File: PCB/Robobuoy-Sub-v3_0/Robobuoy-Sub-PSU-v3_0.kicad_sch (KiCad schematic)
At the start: 83 parts, among them J301 CHRG/DATA, J302 ESC_SB, J303 ESC_BB, J304 ESC_PWR_SB, J305 ESC_PWR_BB, J306 ACCU2, J307 ACCU2, Q301 AO3400A, Q302 AO3401A, Q303 AO3401A, Q304 AO3400A, Q305 AO3400A, Q306 HYG025N04NA1C2, Q307 HYG025N04NA1C2, SW301 On/Off, U301 SN74LV1T34DBV, U302 SN74LV1T34DBV, U303 LMR16020PDDA

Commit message: PCB changes
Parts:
- removed C309: 10u/25V, A_Device:C_0805, symbol Device:C_Small
- removed C315: 100u/10V, Capacitor_SMD:C_1210_3225Metric, symbol Device:C_Small
- removed C317: 100n, A_Device:C_0603, symbol Device:C_Small
- removed J307: ACCU2, A_Connector:AMASS_XT60IPW-M_1x03_P7.20mm_Horizontal, symbol Connector:Conn_01x02_Socket
- removed Q306, Q307: HYG025N04NA1C2, Package_DFN_QFN:PQFN-8-EP_6x5mm_P1.27mm_Generic, symbol Transistor_FET:BSC082N10LSG
- added Q306, Q308: AON6407-MS, Package_DFN_QFN:AO_DFN-8-1EP_5.55x5.2mm_P1.27mm_EP4.12x4.6mm, symbol Transistor_FET:AON6411
- C308: value 10u/25V -> 100n; footprint A_Device:C_0805 -> A_Device:C_0603; LCSC C15850 -> C14663
- J301: footprint A_Connector:AMASS_XT60IPW-M_1x03_P5.50mm_Vertical -> RoundWire_1x03_P5.50mm_Vertical
- J304, J305: footprint A_Connector:AMASS_XT60PW-F_1x02_P7.20mm_Horizontal -> Connector_AMASS:AMASS_XT30U-M_1x02_P5.0mm_Vertical
- J306: footprint A_Connector:AMASS_XT60IPW-M_1x03_P7.20mm_Horizontal -> Connector_AMASS:AMASS_XT30U-M_1x02_P5.0mm_Vertical
- renumbered C310 to C309, C311 to C310, C312 to C311, C313 to C312, C314 to C313, C316 to C315, C318 to C317
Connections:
- net Vbatt: now also Q306.1 (S), Q306.2 (S), Q306.3 (S), Q308.1 (S), Q308.2 (S), Q308.3 (S)
- net buck_sw: now reaches C311.1, D307.1 (K), L301.1, U303.8 (SW)
- net at R326.2, R328.2: now also Q306.4 (G)
- net at R325.2, R327.2: now also Q308.4 (G)
- net at J304.2 (Pin_2): now also Q308.5 (D)
- net at J305.2 (Pin_2): now also Q306.5 (D)
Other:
- moved on the sheet: TP303

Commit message: PCB 3.0 almoste finished Imon calculation added
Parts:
- added C314: 100n, A_Device:C_0603, symbol Device:C_Small
- added R330, R337, R338, R339: 1, Resistor_SMD:R_2512_6332Metric_Pad1.40x3.35mm_HandSolder, symbol Device:R_Small
- added R331, R332: 1.5K, A_Device:R_0603, symbol Device:R_Small
- added R333, R334: 4.6K, A_Device:R_0603, symbol Device:R_Small
- added R335, R336: 10K, A_Device:R_0603, symbol Device:R_Small
- added U304: TL082, Package_SO:SO-8_3.9x4.9mm_P1.27mm, symbol Amplifier_Operational:TL082
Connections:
- net GND: now also C314.2, R330.1, R331.1, R336.1, R337.1, R338.1, R339.1, U304.4 (V-); no longer J306.1 (Pin_1)
- new net: R332.2, R333.1, U304.6 (-)
- new net: R334.2, U304.1, U304.2 (-)
- new net: R335.1, R336.2, U304.3 (+)
- new net: R331.2, R334.1, U304.5 (+)
- new net +3.3V: C314.1, R335.2, U304.8 (V+)
- new net GND1: J306.1 (Pin_1), R330.2, R332.1, R337.2, R338.2, R339.2
- new net Imon: R333.2, U304.7
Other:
- moved on the sheet: J306

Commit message: pcb ready for production
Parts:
- removed J306: ACCU2, Connector_AMASS:AMASS_XT30U-M_1x02_P5.0mm_Vertical, symbol Connector:Conn_01x02_Socket
- removed TP309: GND, TestPoint:TestPoint_Loop_D2.54mm_Drill1.5mm_Beaded, symbol Connector:TestPoint
- added J306: LiPo S6, symbol NicE:LiPo
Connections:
- net GND: now also R332.1; no longer R331.1
- net Vbatt: now also J306.2 (+)
- net GND1: no longer names the net of R330.2, R337.2, R338.2, R339.2
- net GND1: now also R331.1, J306.1 (-); no longer R332.1
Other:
- moved on the sheet: R330, R337, R338, R339

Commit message: Last cosmetic cleanupt
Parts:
- J302, J303, SW301: now not fitted
- TP302: value Vcell -> VSAMP
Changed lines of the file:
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@@
 			)
 		)
-		(property "Value" "Vcell"
+		(property "Value" "VSAMP"
 			(at 111.76 134.62 0)
 			(effects
@@
 		(in_bom yes)
 		(on_board yes)
-		(dnp no)
+		(dnp yes)
 		(fields_autoplaced yes)
 		(property "Reference" "J302"
@@
 		(in_bom yes)
 		(on_board yes)
-		(dnp no)
+		(dnp yes)
 		(property "Reference" "SW301"
 			(at 87.884 253.238 0)
@@
 		(in_bom yes)
 		(on_board yes)
-		(dnp no)
+		(dnp yes)
 		(fields_autoplaced yes)
 		(property "Reference" "J303"

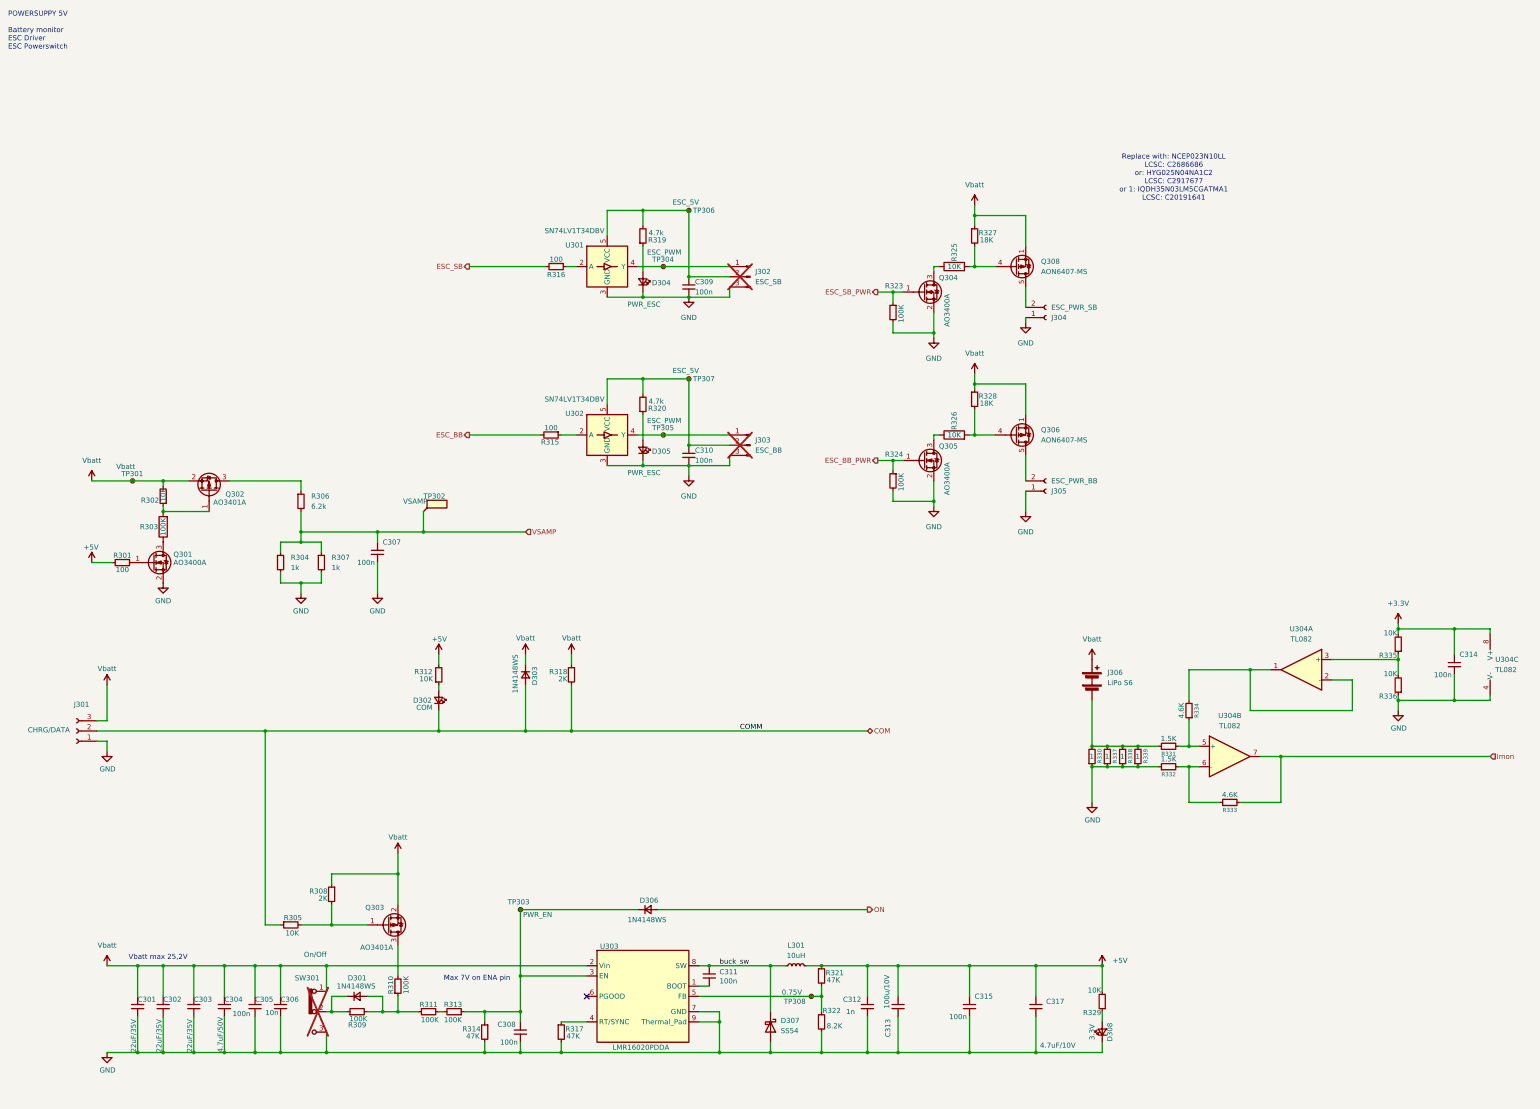
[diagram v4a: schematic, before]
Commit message: Simulation added bms Little improvements BMS Resistor divider added on the gate of the mosfet (Limmeded to +/-20V could be 30V during charging)
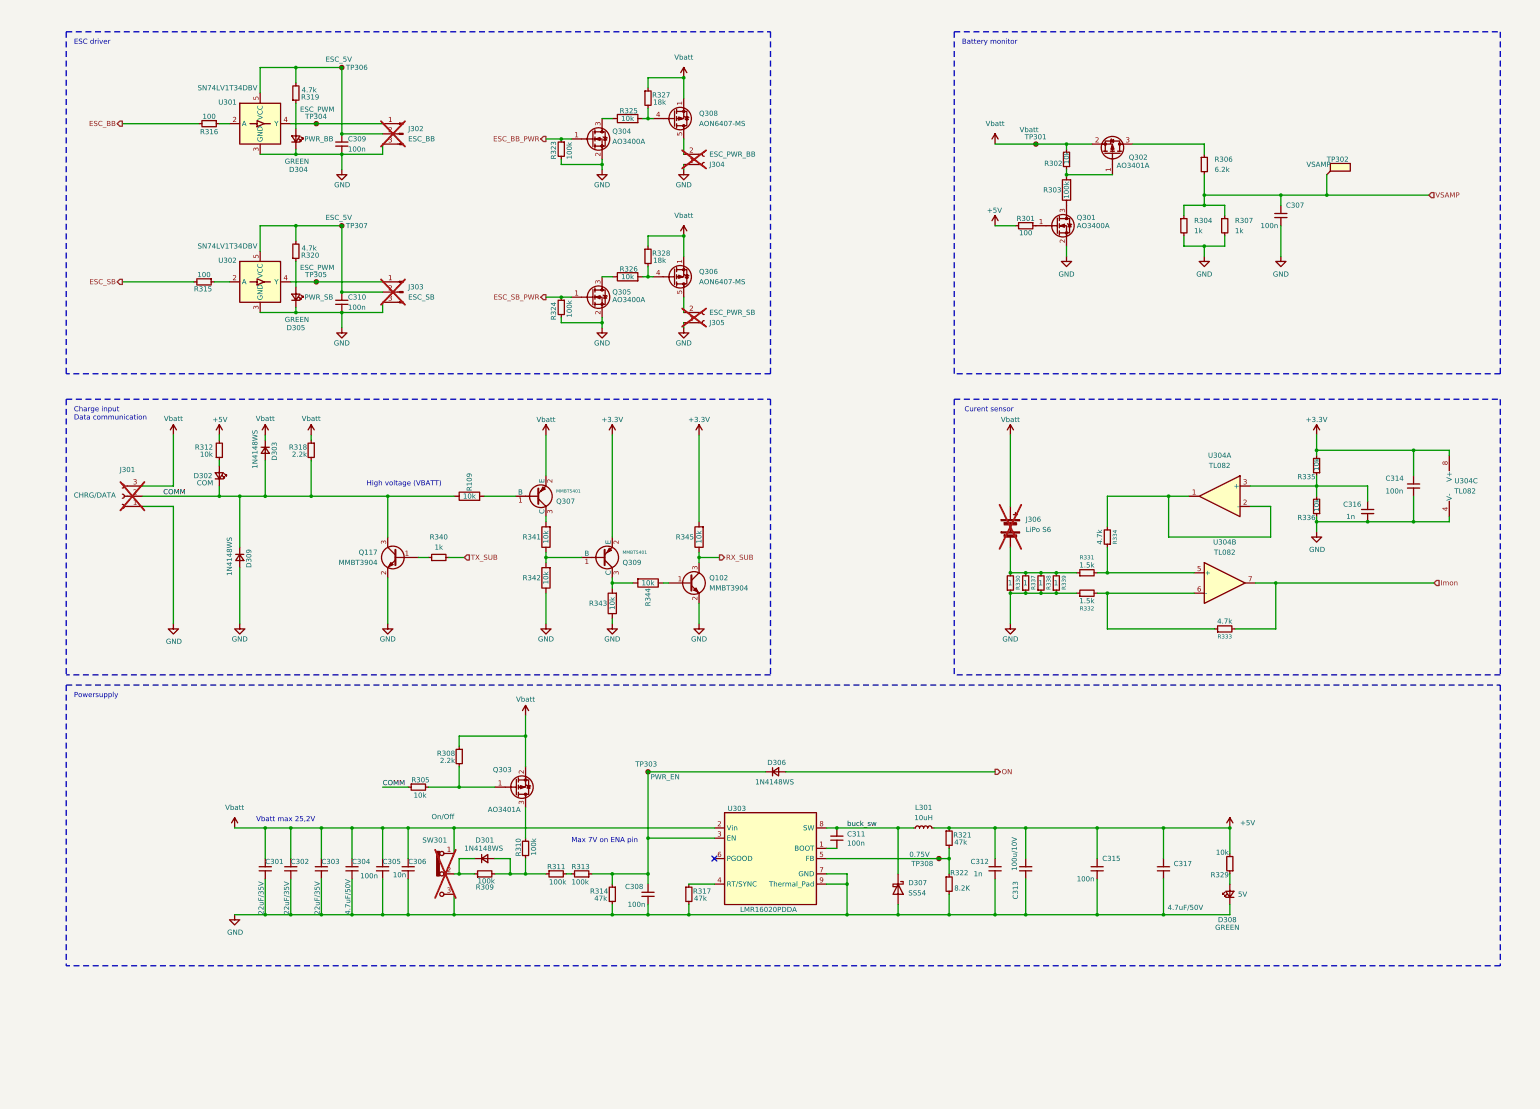
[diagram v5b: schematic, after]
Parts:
- added C316: 1n, A_Device:C_0603, symbol Device:C_Small
- added D309: 1N4148WS, A_Device:D_SOD-323_1.8x1.4x1.15, symbol Device:D_Small
- added Q102, Q117: MMBT3904, Package_TO_SOT_SMD:SOT-23, symbol Transistor_BJT:BC847
- added Q307, Q309: MMBT5401, PCM_JLCPCB:Q_SOT-23, symbol PCM_JLCPCB-Transistors:PNP,MMBT5401
- added R109, R341, R342, R343, R344, R345: 10k, A_Device:R_0603, symbol Device:R
- added R340: 1k, A_Device:R_0603, symbol Device:R_Small
- C317: value 4.7uF/10V -> 4.7uF/50V
- D304: value PWR_ESC -> GREEN; Text (none) -> PWR_BB
- D305: value PWR_ESC -> GREEN; Text (none) -> PWR_SB
- D308: value 3.3V -> GREEN; footprint A_Passive:LED_0805 -> LED_SMD:LED_0603_1608Metric; LCSC C2297 -> C2286; Text (none) -> 5V
- J301, J306: now not fitted; now left out of the parts list
- J302: value ESC_SB -> ESC_BB; now left out of the parts list
- J303: value ESC_BB -> ESC_SB; now left out of the parts list
- J304: value ESC_PWR_SB -> ESC_PWR_BB; now not fitted; now left out of the parts list
- J305: value ESC_PWR_BB -> ESC_PWR_SB; now not fitted; now left out of the parts list
- R302, R305, R312, R325, R326, R329, R335, R336: value 10K -> 10k
- R303, R309, R310, R311, R313, R323, R324: value 100K -> 100k
- R306: LCSC C25804 -> C4260
- R308, R318: value 2K -> 2.2k; LCSC C22975 -> C4190
- R314, R317, R321: value 47K -> 47k
- R327, R328: value 18K -> 18k
- R331, R332: value 1.5K -> 1.5k
- R333, R334: value 4.6K -> 4.7k; LCSC (none) -> C4177
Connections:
- net +3.3V: now also Q309.2 (E), R345.2
- net ESC_BB: now also R316.2; no longer R315.2
- net ESC_BB_PWR: now also Q304.1 (G), R323.1; no longer Q305.1 (G), R324.1
- net ESC_SB: now also R315.2; no longer R316.2
- net ESC_SB_PWR: now also Q305.1 (G), R324.1; no longer Q304.1 (G), R323.1
- net GND: now also C316.2, D309.2 (A), Q102.2 (E), Q117.2 (E), R342.1, R343.1
- net Vbatt: now also Q307.2 (E)
- net at R335.1, R336.2, U304.3 (+): now also C316.1
- net COM renamed COMM
- net COMM: now also D309.1 (K), Q117.3 (C), R109.1
- new net: Q309.1 (B), R341.1, R342.2
- new net: Q309.3 (C), R343.2, R344.2
- new net: Q102.1 (B), R344.1
- new net: Q307.3 (C), R341.2
- new net: Q117.1 (B), R340.1
- new net: Q307.1 (B), R109.2
- new net RX_SUB: Q102.3 (C), R345.1
- new net TX_SUB: R340.2
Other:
- note added: "Battery monitor"
- note added: "Charge input Data communication"
- note added: "Curent sensor"
- note added: "ESC driver"
- note added: "High voltage (VBATT)"
- note added: "Powersupply"
- note removed: "POWERSUPPY 5V Battery monitor ESC Driver ESC Powerswitch"
- note removed: "Replace with: NCEP023N10LL LCSC: C2686686 or: HYG025N04NA1C2 LCSC: C2917677 or 1: IQDH35N03LM5CGATMA1 LCSC: C20191641"
- moved on the sheet: C301, C302, C303, C304, C305, C306, C307, C308, C309, C310, C311, C312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

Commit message: Heel veel AI veranderingen.
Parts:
- added D310: 1N4148WS, A_Device:D_SOD-323_1.8x1.4x1.15, symbol Device:D_Small
- added R346: 100, A_Device:R_0603, symbol Device:R_Small
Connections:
- net +3.3V: now also D310.1 (K); no longer C314.1, U304.8 (V+)
- net +5V: now also C314.1, U304.8 (V+)
- net Imon: now also D310.2 (A), R346.1; no longer R333.2, U304.7
- new net: R333.2, R346.2, U304.7
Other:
- note added: "Imon 0.10V = -20A 1.65V = 0A 3.20V = 20A"

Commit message: BMS asd SUB orderd at JLCPCB
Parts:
- D304, D305, D308: LCSC C2286 -> C12624
- R303, R309, R310, R311, R313, R323, R324: LCSC C25804 -> C25803
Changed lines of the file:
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@@
 			)
 		)
-		(property "LCSC" "C25804"
+		(property "LCSC" "C25803"
 			(at 129.286 227.076 0)
 			(effects
@@
 			)
 		)
-		(property "LCSC" "C25804"
+		(property "LCSC" "C25803"
 			(at 159.004 227.076 0)
 			(effects
@@
 			)
 		)
-		(property "LCSC" "C25804"
+		(property "LCSC" "C25803"
 			(at 276.86 57.15 0)
 			(effects
@@
 			)
 		)
-		(property "LCSC" "C2286"
+		(property "LCSC" "C12624"
 			(at 85.09 83.82 0)
 			(effects
@@
 			)
 		)
-		(property "LCSC" "C25804"
+		(property "LCSC" "C25803"
 			(at 147.066 227.584 0)
 			(effects
@@
 			)
 		)
-		(property "LCSC" "C25804"
+		(property "LCSC" "C25803"
 			(at 142.494 223.774 0)
 			(effects
@@
 			)
 		)
-		(property "LCSC" "C25804"
+		(property "LCSC" "C25803"
 			(at 150.876 44.196 0)
 			(effects
@@
 			)
 		)
-		(property "LCSC" "C25804"
+		(property "LCSC" "C25803"
 			(at 150.876 83.566 0)
 			(effects
@@
 			)
 		)
-		(property "LCSC" "C2286"
+		(property "LCSC" "C12624"
 			(at 317.5 232.41 0)
 			(effects
@@
 			)
 		)
-		(property "LCSC" "C2286"
+		(property "LCSC" "C12624"
 			(at 85.09 44.45 0)
 			(effects

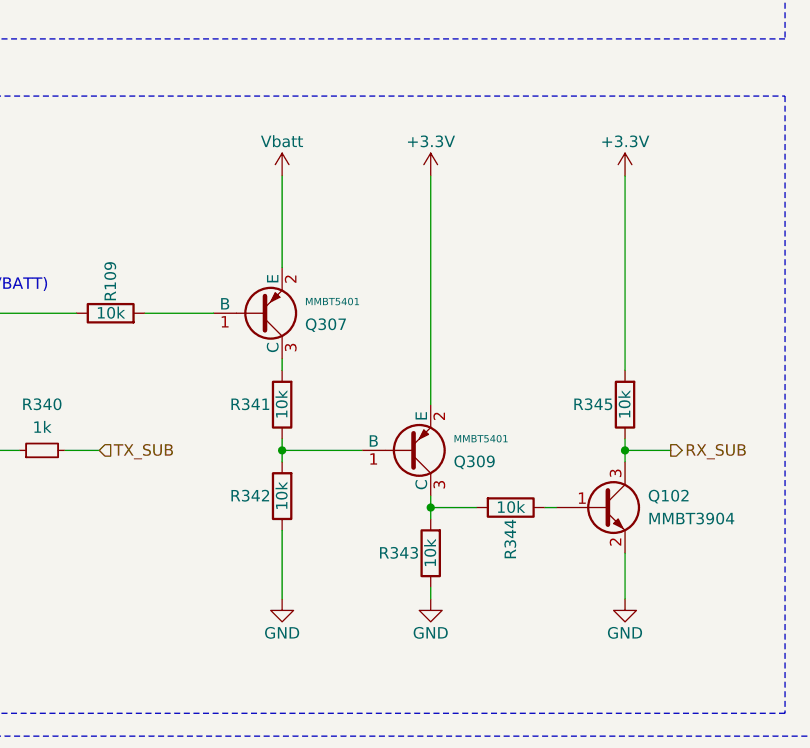
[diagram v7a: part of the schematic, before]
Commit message: docs: update PCB schematics and add ICM20948 datasheet
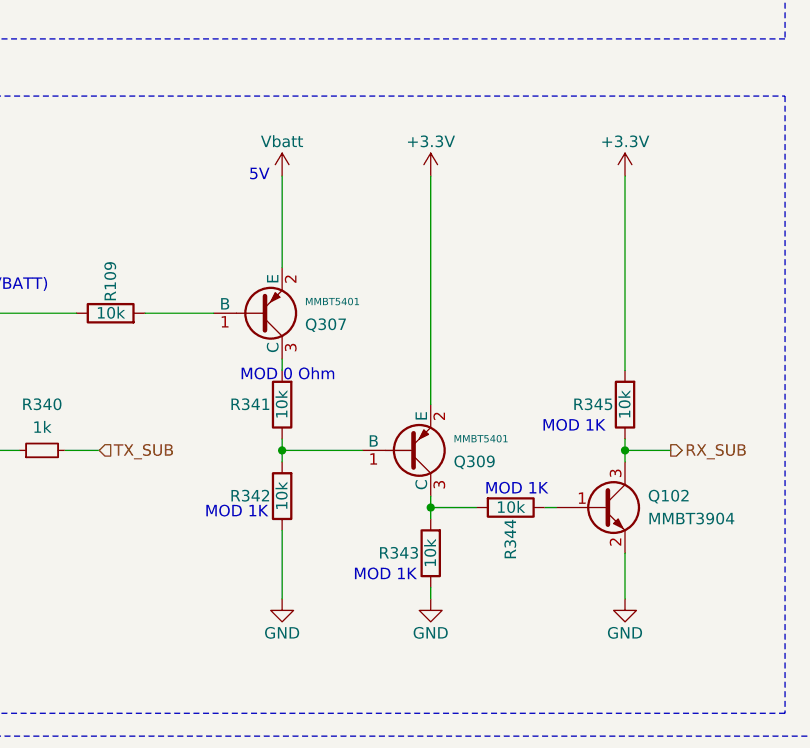
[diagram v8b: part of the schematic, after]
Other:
- note added: "5V"
- note added: "MOD 0 Ohm"
- note added: "MOD 1K"
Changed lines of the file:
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@@
 		(company "NicE Engineering")
+	)
+	(text "MOD 0 Ohm"
+		(exclude_from_sim no)
+		(at 147.955 140.335 0)
+		(effects
+			(font
+				(size 1.27 1.27)
+			)
+		)
 	)
 	(text "ESC driver"
@@
 		)
 	)
+	(text "MOD 1K"
+		(exclude_from_sim no)
+		(at 179.705 146.05 0)
+		(effects
+			(font
+				(size 1.27 1.27)
+			)
+		)
+	)
+	(text "MOD 1K"
+		(exclude_from_sim no)
+		(at 173.355 153.035 0)
+		(effects
+			(font
+				(size 1.27 1.27)
+			)
+		)
+	)
+	(text "MOD 1K"
+		(exclude_from_sim no)
+		(at 142.24 155.575 0)
+		(effects
+			(font
+				(size 1.27 1.27)
+			)
+		)
+	)
 	(text "High voltage (VBATT)"
 		(exclude_from_sim no)
 		(at 112.014 130.302 0)
+		(effects
+			(font
+				(size 1.27 1.27)
+			)
+		)
+	)
+	(text "5V"
+		(exclude_from_sim no)
+		(at 144.78 118.11 0)
 		(effects
 			(font
@@
 		)
 	)
+	(text "MOD 1K"
+		(exclude_from_sim no)
+		(at 158.75 162.56 0)
+		(effects
+			(font
+				(size 1.27 1.27)
+			)
+		)
+	)
